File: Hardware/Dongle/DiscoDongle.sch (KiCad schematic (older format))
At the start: 22 parts, among them J1 RJ45, P1 USB_B, P2 FTDI, U1 FT232RL, U2 ISL81487E

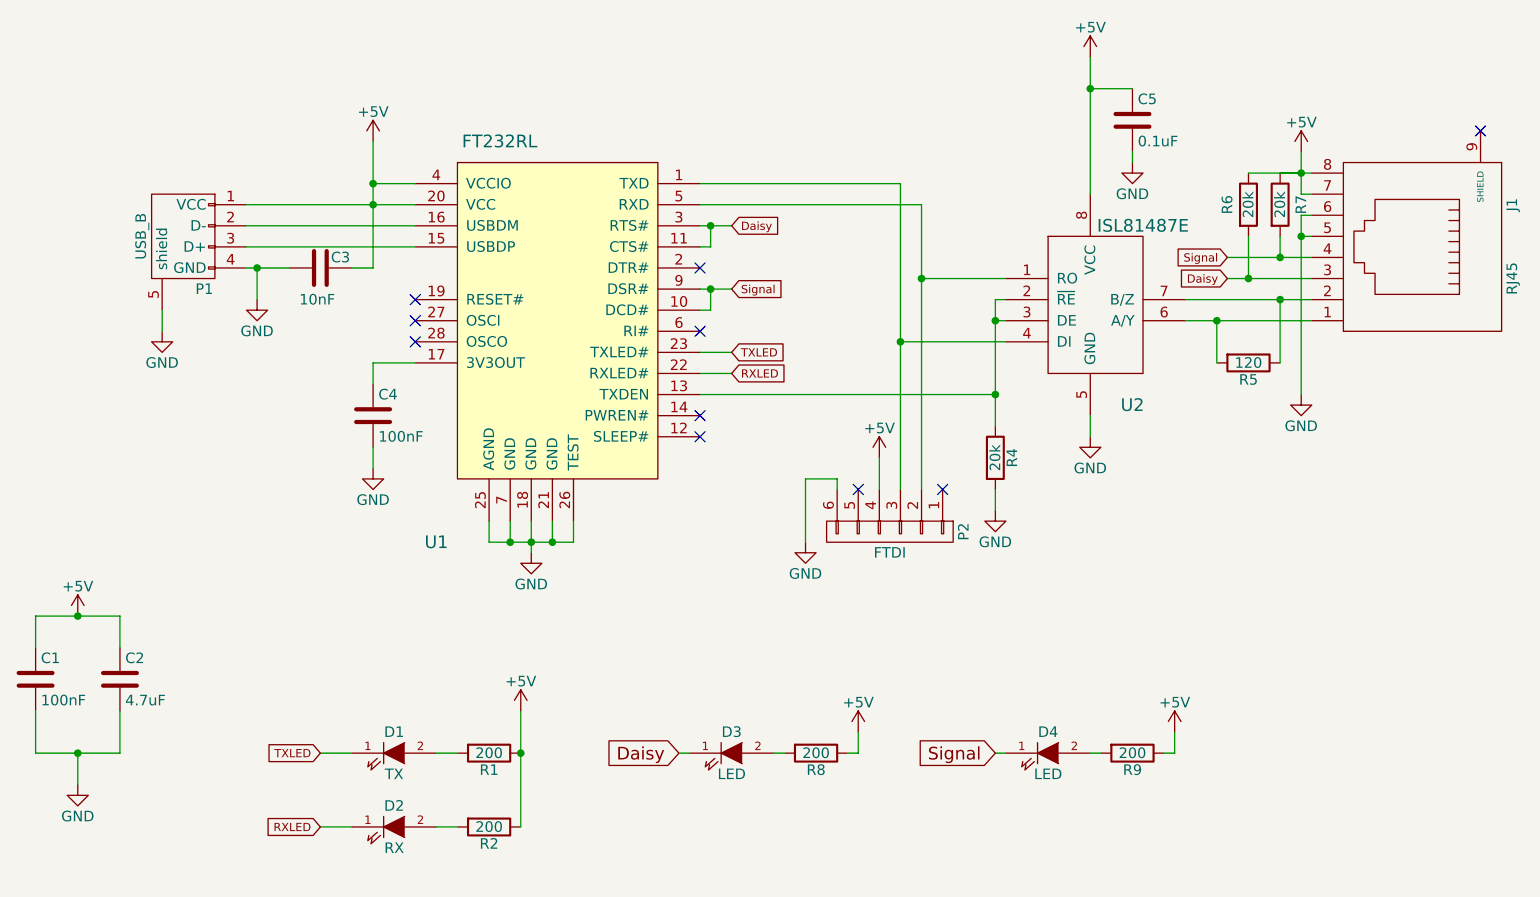
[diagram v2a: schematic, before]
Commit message: DiscoDongle - Rev5 - Move components to bottom.
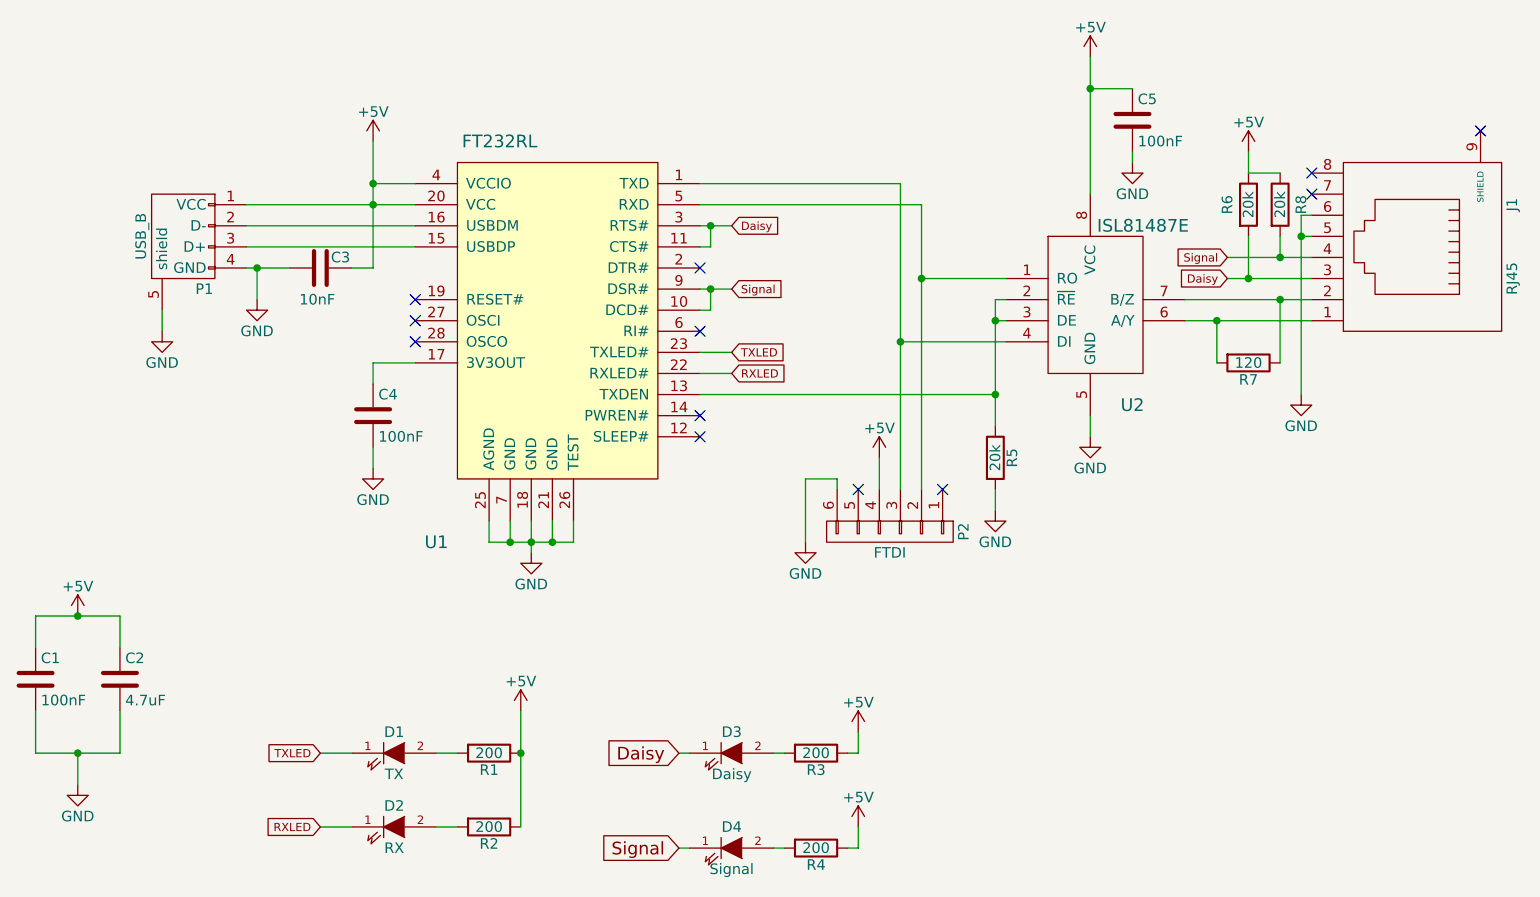
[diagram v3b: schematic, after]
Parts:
- C5: value 0.1uF -> 100nF
- D3: value LED -> Daisy
- D4: value LED -> Signal
- J1: footprint DongleParts:RJ45 -> Connect:RJ45_8
- renumbered R8 to R3, R9 to R4, R4 to R5, R5 to R7, R7 to R8
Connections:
- net +5V: no longer J1.7, J1.8
- no-connect marks 10 -> 12
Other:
- moved on the sheet: D4, R4
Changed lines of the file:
@@
 $EndComp
 $Comp
-L +5V #PWR01
+L +5V #PWR5
 U 1 1 57468E3D
 P 2800 1450
-F 0 "#PWR01" H 2800 1300 50  0001 C CNN
+F 0 "#PWR5" H 2800 1300 50  0001 C CNN
 F 1 "+5V" H 2800 1590 50  0000 C CNN
 F 2 "" H 2800 1450 50  0000 C CNN
@@
 F 0 "J1" H 7900 2450 50  0000 C CNN
 F 1 "RJ45" H 7550 2450 50  0000 C CNN
-F 2 "DongleParts:RJ45" H 7700 1950 50  0001 C CNN
+F 2 "Connect:RJ45_8" H 7700 1950 50  0001 C CNN
 F 3 "" H 7700 1950 50  0000 C CNN
 	1    7700 1950
@@
 $EndComp
 $Comp
-L R R4
+L R R5
 U 1 1 574695A2
 P 5750 2950
-F 0 "R4" V 5830 2950 50  0000 C CNN
+F 0 "R5" V 5830 2950 50  0000 C CNN
 F 1 "20k" V 5750 2950 50  0000 C CNN
 F 2 "Resistors_SMD:R_0805" V 5680 2950 50  0001 C CNN
@@
 $EndComp
 $Comp
-L +5V #PWR02
+L +5V #PWR12
 U 1 1 57469E82
 P 5200 2950
-F 0 "#PWR02" H 5200 2800 50  0001 C CNN
+F 0 "#PWR12" H 5200 2800 50  0001 C CNN
 F 1 "+5V" H 5200 3090 50  0000 C CNN
 F 2 "" H 5200 2950 50  0000 C CNN
@@
 $EndComp
 $Comp
-L +5V #PWR03
+L +5V #PWR14
 U 1 1 5746A496
 P 6200 1050
-F 0 "#PWR03" H 6200 900 50  0001 C CNN
+F 0 "#PWR14" H 6200 900 50  0001 C CNN
 F 1 "+5V" H 6200 1190 50  0000 C CNN
 F 2 "" H 6200 1050 50  0000 C CNN
@@
 $EndComp
 $Comp
-L +5V #PWR04
+L +5V #PWR7
 U 1 1 5746ACA4
 P 3500 4150
-F 0 "#PWR04" H 3500 4000 50  0001 C CNN
+F 0 "#PWR7" H 3500 4000 50  0001 C CNN
 F 1 "+5V" H 3500 4290 50  0000 C CNN
 F 2 "" H 3500 4150 50  0000 C CNN
@@
 $EndComp
 $Comp
-L R R5
+L R R7
 U 1 1 5746B006
 P 6950 2500
-F 0 "R5" V 7030 2500 50  0000 C CNN
+F 0 "R7" V 7030 2500 50  0000 C CNN
 F 1 "120" V 6950 2500 50  0000 C CNN
 F 2 "Resistors_SMD:R_0805" V 6880 2500 50  0001 C CNN
@@
 $EndComp
 $Comp
-L +5V #PWR05
+L +5V #PWR17
 U 1 1 5746B3A8
-P 7200 1500
-F 0 "#PWR05" H 7200 1350 50  0001 C CNN
-F 1 "+5V" H 7200 1640 50  0000 C CNN
-F 2 "" H 7200 1500 50  0000 C CNN
-F 3 "" H 7200 1500 50  0000 C CNN
-	1    7200 1500
+P 6950 1500
+F 0 "#PWR17" H 6950 1350 50  0001 C CNN
+F 1 "+5V" H 6950 1640 50  0000 C CNN
+F 2 "" H 6950 1500 50  0000 C CNN
+F 3 "" H 6950 1500 50  0000 C CNN
+	1    6950 1500
 	1    0    0    -1
 $EndComp
@@
 P 6400 1350
 F 0 "C5" H 6425 1450 50  0000 L CNN
-F 1 "0.1uF" H 6425 1250 50  0000 L CNN
+F 1 "100nF" H 6425 1250 50  0000 L CNN
 F 2 "Capacitors_SMD:C_0805" H 6438 1200 50  0001 C CNN
 F 3 "" H 6400 1350 50  0000 C CNN
@@
 $EndComp
 $Comp
-L +5V #PWR07
+L +5V #PWR1
 U 1 1 5746D453
 P 1400 3700
-F 0 "#PWR07" H 1400 3550 50  0001 C CNN
+F 0 "#PWR1" H 1400 3550 50  0001 C CNN
 F 1 "+5V" H 1400 3840 50  0000 C CNN
 F 2 "" H 1400 3700 50  0000 C CNN
@@
 NoConn ~ 5100 3100
 $Comp
-L R R7
+L R R8
 U 1 1 5747F3E8
 P 7100 1750
-F 0 "R7" V 7200 1750 50  0000 C CNN
+F 0 "R8" V 7200 1750 50  0000 C CNN
 F 1 "20k" V 7100 1750 50  0000 C CNN
 F 2 "Resistors_SMD:R_0805" V 7030 1750 50  0001 C CNN
@@
 P 4500 4350
 F 0 "D3" H 4500 4450 50  0000 C CNN
-F 1 "LED" H 4500 4250 50  0000 C CNN
+F 1 "Daisy" H 4500 4250 50  0000 C CNN
 F 2 "LEDs:LED_0805" H 4500 4350 50  0001 C CNN
 F 3 "" H 4500 4350 50  0000 C CNN
@@
 $EndComp
 $Comp
-L R R8
+L R R3
 U 1 1 5748F6BB
 P 4900 4350
-F 0 "R8" V 4980 4350 50  0000 C CNN
+F 0 "R3" V 4980 4350 50  0000 C CNN
 F 1 "200" V 4900 4350 50  0000 C CNN
 F 2 "Resistors_SMD:R_0805" V 4830 4350 50  0001 C CNN
@@
 $EndComp
 $Comp
-L GND #PWR09
+L GND #PWR2
 U 1 1 5748FDFC
 P 1400 4500
-F 0 "#PWR09" H 1400 4250 50  0001 C CNN
+F 0 "#PWR2" H 1400 4250 50  0001 C CNN
 F 1 "GND" H 1400 4350 50  0000 C CNN
 F 2 "" H 1400 4500 50  0000 C CNN
@@
 $EndComp
 $Comp
-L GND #PWR010
+L GND #PWR6
 U 1 1 5748FFF1
 P 2800 3000
-F 0 "#PWR010" H 2800 2750 50  0001 C CNN
+F 0 "#PWR6" H 2800 2750 50  0001 C CNN
 F 1 "GND" H 2800 2850 50  0000 C CNN
 F 2 "" H 2800 3000 50  0000 C CNN
@@
 $EndComp
 $Comp
-L GND #PWR011
+L GND #PWR4
 U 1 1 57490056
 P 2250 2200
-F 0 "#PWR011" H 2250 1950 50  0001 C CNN
+F 0 "#PWR4" H 2250 1950 50  0001 C CNN
 F 1 "GND" H 2250 2050 50  0000 C CNN
 F 2 "" H 2250 2200 50  0000 C CNN
@@
 $EndComp
 $Comp
-L GND #PWR012
+L GND #PWR3
 U 1 1 574900BB
 P 1800 2350
-F 0 "#PWR012" H 1800 2100 50  0001 C CNN
+F 0 "#PWR3" H 1800 2100 50  0001 C CNN
 F 1 "GND" H 1800 2200 50  0000 C CNN
 F 2 "" H 1800 2350 50  0000 C CNN
@@
 $EndComp
 $Comp
-L GND #PWR013
+L GND #PWR8
 U 1 1 57490134
 P 3550 3400
-F 0 "#PWR013" H 3550 3150 50  0001 C CNN
+F 0 "#PWR8" H 3550 3150 50  0001 C CNN
 F 1 "GND" H 3550 3250 50  0000 C CNN
 F 2 "" H 3550 3400 50  0000 C CNN
@@
 $EndComp
 $Comp
-L GND #PWR014
+L GND #PWR9
 U 1 1 57490211
 P 4850 3350
-F 0 "#PWR014" H 4850 3100 50  0001 C CNN
+F 0 "#PWR9" H 4850 3100 50  0001 C CNN
 F 1 "GND" H 4850 3200 50  0000 C CNN
 F 2 "" H 4850 3350 50  0000 C CNN
@@
 $EndComp
 $Comp
-L GND #PWR015
+L GND #PWR13
 U 1 1 5749029E
 P 5750 3200
-F 0 "#PWR015" H 5750 2950 50  0001 C CNN
+F 0 "#PWR13" H 5750 2950 50  0001 C CNN
 F 1 "GND" H 5750 3050 50  0000 C CNN
 F 2 "" H 5750 3200 50  0000 C CNN
@@
 $EndComp
 $Comp
-L GND #PWR016
+L GND #PWR15
 U 1 1 57490303
 P 6200 2850
-F 0 "#PWR016" H 6200 2600 50  0001 C CNN
+F 0 "#PWR15" H 6200 2600 50  0001 C CNN
 F 1 "GND" H 6200 2700 50  0000 C CNN
 F 2 "" H 6200 2850 50  0000 C CNN
@@
 $EndComp
 $Comp
-L GND #PWR017
+L GND #PWR16
 U 1 1 57490430
 P 6400 1550
-F 0 "#PWR017" H 6400 1300 50  0001 C CNN
+F 0 "#PWR16" H 6400 1300 50  0001 C CNN
 F 1 "GND" H 6400 1400 50  0000 C CNN
 F 2 "" H 6400 1550 50  0000 C CNN
@@
 $EndComp
 $Comp
-L GND #PWR018
+L GND #PWR18
 U 1 1 5749091D
 P 7200 2650
-F 0 "#PWR018" H 7200 2400 50  0001 C CNN
+F 0 "#PWR18" H 7200 2400 50  0001 C CNN
 F 1 "GND" H 7200 2500 50  0000 C CNN
 F 2 "" H 7200 2650 50  0000 C CNN
@@
 	1    0    0    -1
 $EndComp
-Text GLabel 5750 4350 0    60   Input ~ 0
+Text GLabel 4250 4800 0    60   Input ~ 0
 Signal
 $Comp
 L LED D4
 U 1 1 57490E65
-P 6000 4350
-F 0 "D4" H 6000 4450 50  0000 C CNN
-F 1 "LED" H 6000 4250 50  0000 C CNN
-F 2 "LEDs:LED_0805" H 6000 4350 50  0001 C CNN
-F 3 "" H 6000 4350 50  0000 C CNN
-	1    6000 4350
-	1    0    0    -1
-$EndComp
-$Comp
-L R R9
+P 4500 4800
+F 0 "D4" H 4500 4900 50  0000 C CNN
+F 1 "Signal" H 4500 4700 50  0000 C CNN
+F 2 "LEDs:LED_0805" H 4500 4800 50  0001 C CNN
+F 3 "" H 4500 4800 50  0000 C CNN
+	1    4500 4800
+	1    0    0    -1
+$EndComp
+$Comp
+L R R4
 U 1 1 57490EAE
-P 6400 4350
-F 0 "R9" V 6480 4350 50  0000 C CNN
-F 1 "200" V 6400 4350 50  0000 C CNN
-F 2 "Resistors_SMD:R_0805" V 6330 4350 50  0001 C CNN
-F 3 "" H 6400 4350 50  0000 C CNN
-	1    6400 4350
+P 4900 4800
+F 0 "R4" V 4980 4800 50  0000 C CNN
+F 1 "200" V 4900 4800 50  0000 C CNN
+F 2 "Resistors_SMD:R_0805" V 4830 4800 50  0001 C CNN
+F 3 "" H 4900 4800 50  0000 C CNN
+	1    4900 4800
 	0    1    1    0
 $EndComp
 $Comp
-L +5V #PWR019
+L +5V #PWR11
 U 1 1 57490EF7
-P 6600 4250
-F 0 "#PWR019" H 6600 4100 50  0001 C CNN
-F 1 "+5V" H 6600 4390 50  0000 C CNN
-F 2 "" H 6600 4250 50  0000 C CNN
-F 3 "" H 6600 4250 50  0000 C CNN
-	1    6600 4250
+P 5100 4700
+F 0 "#PWR11" H 5100 4550 50  0001 C CNN
+F 1 "+5V" H 5100 4840 50  0000 C CNN
+F 2 "" H 5100 4700 50  0000 C CNN
+F 3 "" H 5100 4700 50  0000 C CNN
+	1    5100 4700
 	1    0    0    -1
 $EndComp
@@
 	2800 2900 2800 3000
 Wire Wire Line
-	4350 2650 5750 2650
+	5750 2650 4350 2650
 Wire Wire Line
 	5750 2200 5750 2800
@@
 Connection ~ 7200 1900
 Wire Wire Line
-	7200 1700 7250 1700
-Wire Wire Line
-	7200 1500 7200 1700
-Wire Wire Line
-	7100 1600 7250 1600
-Connection ~ 7200 1600
-Wire Wire Line
 	4350 2450 4500 2450
 Wire Wire Line
@@
 	4700 4350 4750 4350
 Wire Wire Line
-	6550 4350 6600 4350
-Wire Wire Line
-	6600 4350 6600 4250
-Wire Wire Line
-	6250 4350 6200 4350
-Wire Wire Line
-	5750 4350 5800 4350
+	5050 4800 5100 4800
+Wire Wire Line
+	5100 4800 5100 4700
+Wire Wire Line
+	4750 4800 4700 4800
+Wire Wire Line
+	4250 4800 4300 4800
 Wire Wire Line
 	6200 2750 6200 2850
@@
 	6950 1900 6950 2100
 Connection ~ 6950 2100
-Wire Wire Line
-	6950 1600 7200 1600
 Connection ~ 4400 1850
 Wire Wire Line
@@
 	4350 1950 4400 1950
 $Comp
-L +5V #PWR?
+L +5V #PWR10
 U 1 1 576751A3
 P 5100 4250
-F 0 "#PWR?" H 5100 4100 50  0001 C CNN
+F 0 "#PWR10" H 5100 4100 50  0001 C CNN
 F 1 "+5V" H 5100 4390 50  0000 C CNN
 F 2 "" H 5100 4250 50  0000 C CNN
@@
 Connection ~ 5750 2300
 NoConn ~ 4350 2750
+Wire Wire Line
+	6950 1600 6950 1500
+Wire Wire Line
+	7100 1600 6950 1600
+NoConn ~ 7250 1600
+NoConn ~ 7250 1700
 $EndSCHEMATC

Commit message: Simplify daily/signal connections. Remove FTDI headers.
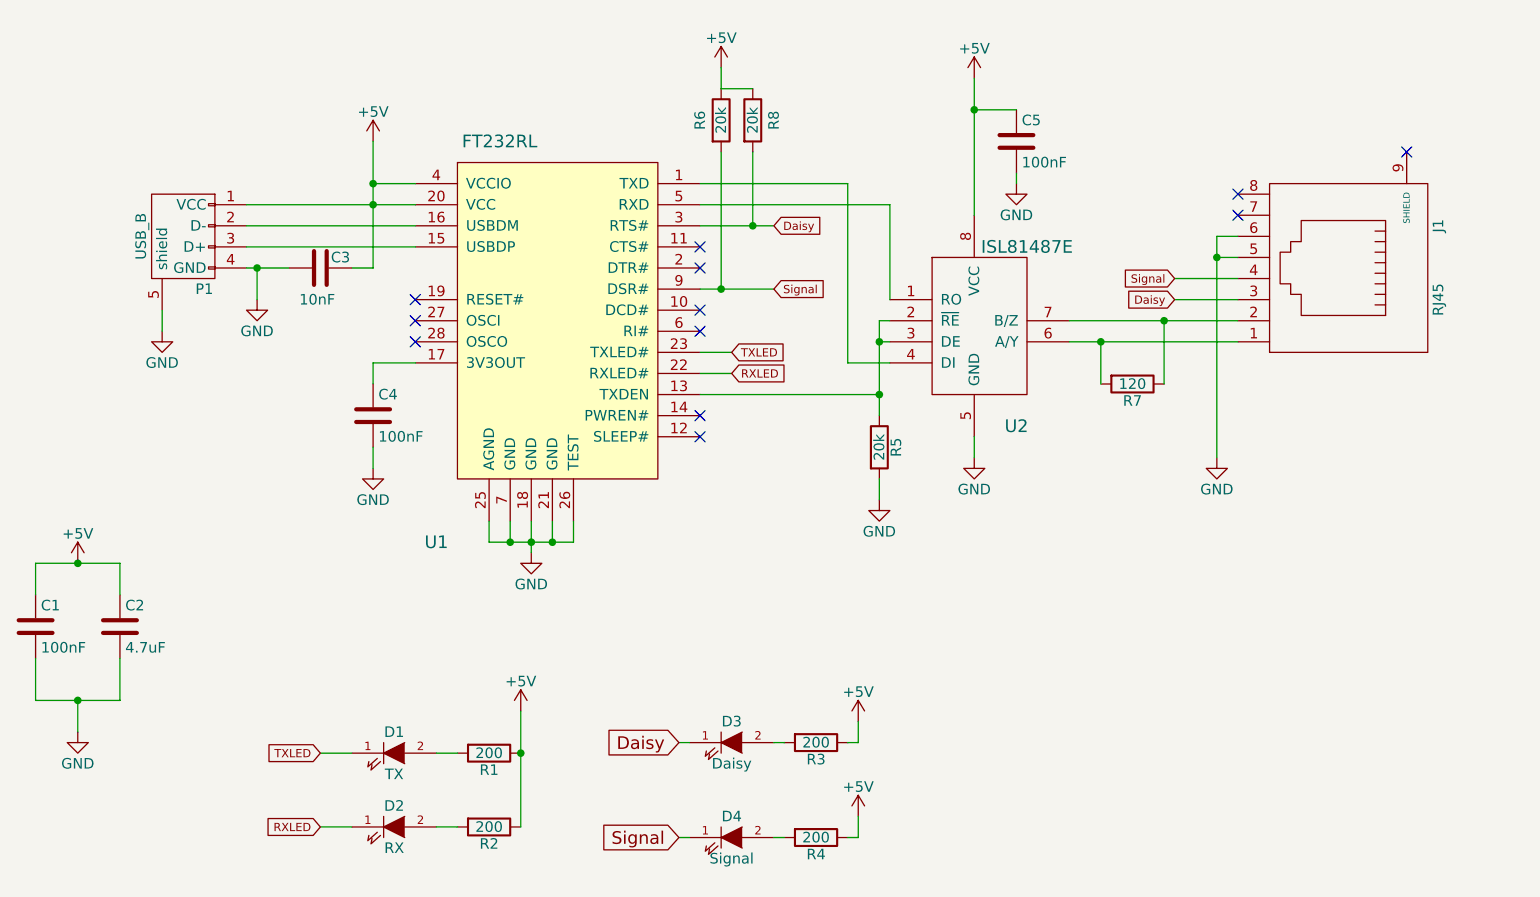
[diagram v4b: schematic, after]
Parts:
- removed P2: FTDI, Pin_Headers:Pin_Header_Straight_1x06, symbol CONN_01X06
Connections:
- net Daisy: now also R8.2; no longer R6.2, U1.11 (CTS#)
- net Signal: now also R6.2; no longer R8.2, U1.10 (DCD#)
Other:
- moved on the sheet: C1, C2, C5, D3, D4, J1, R3, R4, R5, R6, R7, R8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

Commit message: Fix USB position.
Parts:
- D1, D2, D3, D4: symbol LED -> LED-RESCUE-DiscoDongle
- P1: symbol USB_B -> USB_B-RESCUE-DiscoDongle
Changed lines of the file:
@@
 $EndComp
 $Comp
-L USB_B P1
+L USB_B-RESCUE-DiscoDongle P1
 U 1 1 57468D47
 P 1900 1950
@@
 $EndComp
 $Comp
-L LED D1
+L LED-RESCUE-DiscoDongle D1
 U 1 1 5746A4EF
 P 2900 4350
@@
 $EndComp
 $Comp
-L LED D2
+L LED-RESCUE-DiscoDongle D2
 U 1 1 5746A53E
 P 2900 4700
@@
 Daisy
 $Comp
-L LED D3
+L LED-RESCUE-DiscoDongle D3
 U 1 1 5748F519
 P 4500 4300
@@
 Signal
 $Comp
-L LED D4
+L LED-RESCUE-DiscoDongle D4
 U 1 1 57490E65
 P 4500 4750
